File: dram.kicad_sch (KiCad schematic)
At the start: 21 parts, among them J2 74157, J3 74157, J7 74LS280, K10 74LS08, K9 4164, U10 4164, U11 4164, U12 4164, U13 4164, U4 74LS04, U6 4164, U7 4164, U8 4164, U9 4164

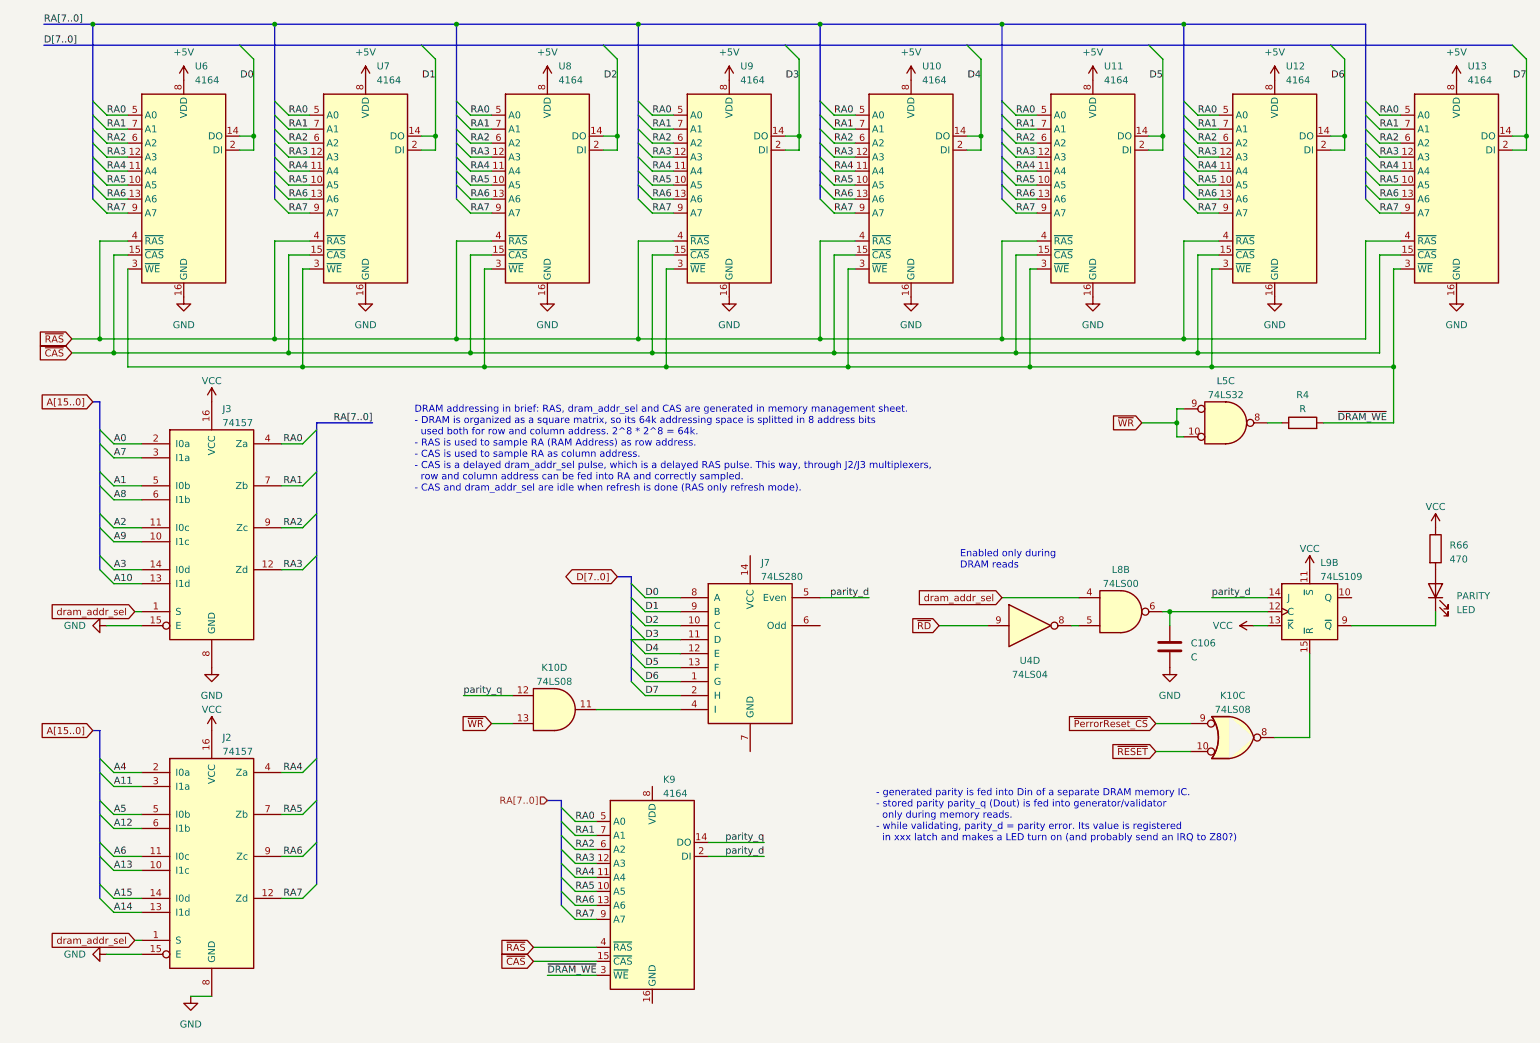
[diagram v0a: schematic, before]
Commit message: Components renaming according to the Uxy convention.
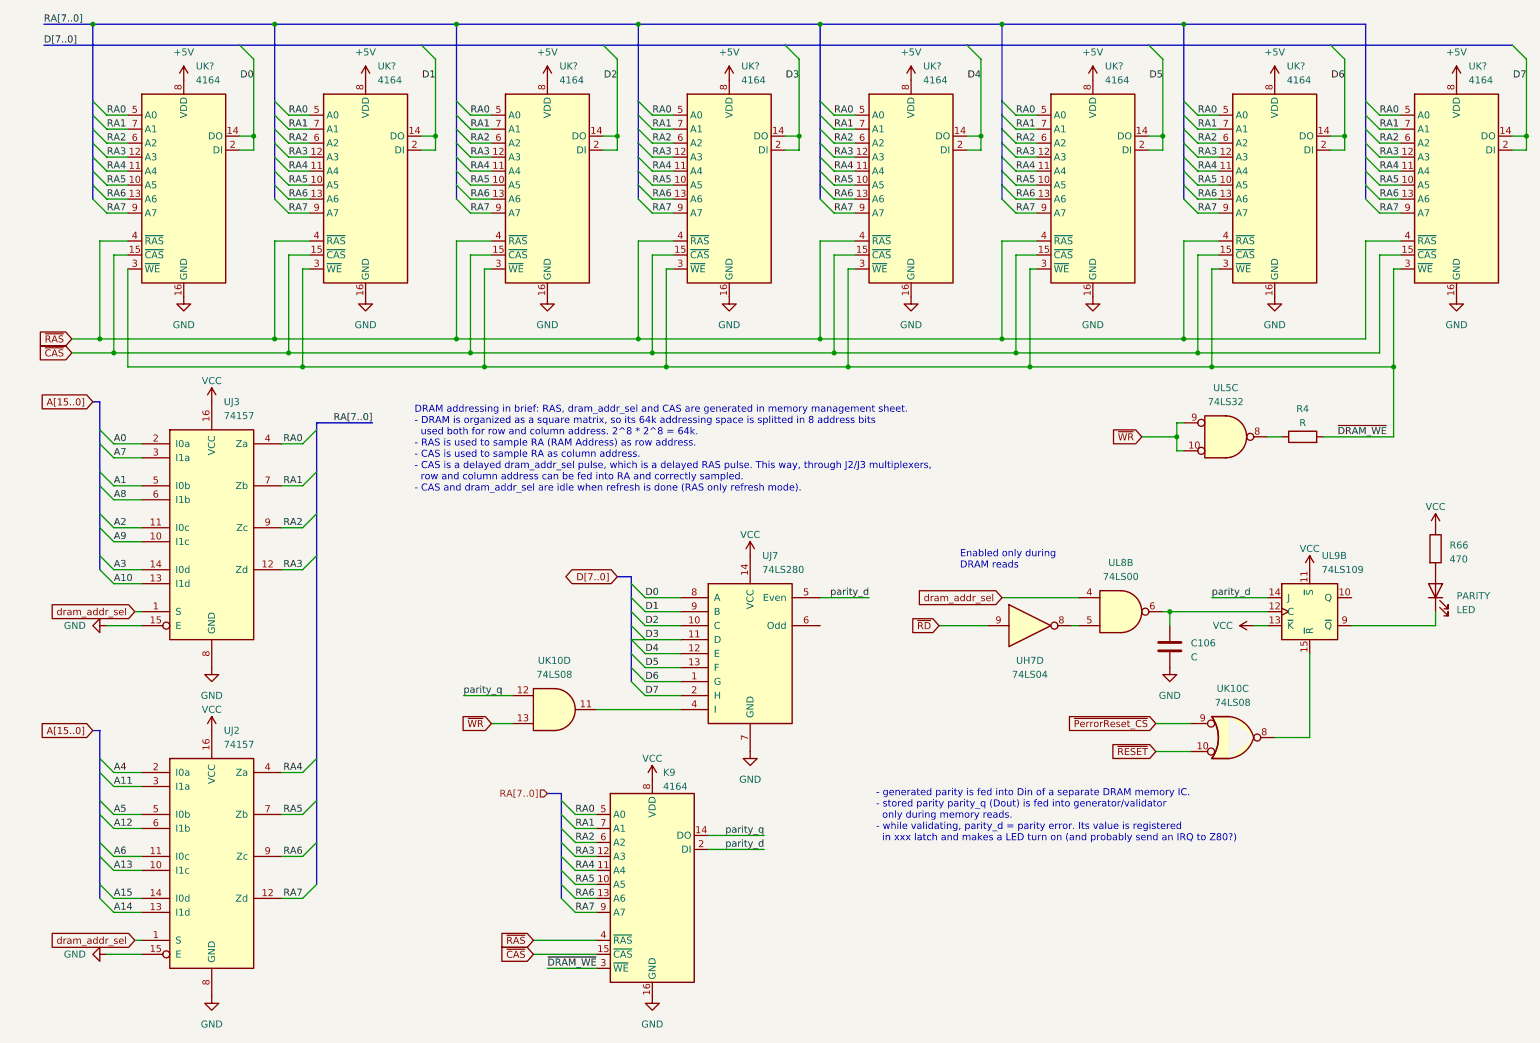
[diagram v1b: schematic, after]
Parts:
- renumbered U4 to UH7, J2 to UJ2, J3 to UJ3, J7 to UJ7, K10 to UK10, U7 to UK?, U13 to UK?, U10 to UK?, U11 to UK?, U12 to UK?, U9 to UK?, U8 to UK?, U6 to UK?, L5 to UL5, L8 to UL8, L9 to UL9
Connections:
- net GND: now also K9.16 (GND), UJ7.7 (GND)
- net VCC: now also K9.8 (VDD), UJ7.14 (VCC)
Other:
- moved on the sheet: K9, R4, UL5C

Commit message: VCC -> +5V
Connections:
- net VCC is gone; now on net +5V: K9.8 (VDD), R66.1, UJ2.16 (VCC), UJ3.16 (VCC), UJ7.14 (VCC), UL9.11 (~{S}), UL9.13 (~{K})
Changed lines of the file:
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@@
     )
   )
-  (symbol (lib_id "power:VCC") (at 233.68 124.46 90) (unit 1)
-    (in_bom yes) (on_board yes) (dnp no) (fields_autoplaced)
-    (property "Reference" "#PWR010" (at 237.49 124.46 0)
-      (effects (font (size 1.27 1.27)) hide)
-    )
-    (property "Value" "VCC" (at 229.87 124.46 90)
+  (symbol (lib_name "+5V_1") (lib_id "power:+5V") (at 233.68 124.46 90) (unit 1)
+    (in_bom yes) (on_board yes) (dnp no) (fields_autoplaced)
+    (property "Reference" "#PWR?" (at 237.49 124.46 0)
+      (effects (font (size 1.27 1.27)) hide)
+    )
+    (property "Value" "+5V" (at 229.87 124.46 90)
       (effects (font (size 1.27 1.27)) (justify left))
     )
@@
       (project "ceda"
         (path "/12a6dbe3-008d-4c5b-88f6-9f1c816060be/f05e0b09-5f96-4638-8985-dbb50d0f6ef2"
-          (reference "#PWR010") (unit 1)
+          (reference "#PWR?") (unit 1)
         )
       )
@@
     )
   )
-  (symbol (lib_id "power:VCC") (at 44.45 143.51 0) (unit 1)
-    (in_bom yes) (on_board yes) (dnp no) (fields_autoplaced)
-    (property "Reference" "#PWR031" (at 44.45 147.32 0)
-      (effects (font (size 1.27 1.27)) hide)
-    )
-    (property "Value" "VCC" (at 44.45 139.7 0)
+  (symbol (lib_name "+5V_2") (lib_id "power:+5V") (at 44.45 143.51 0) (unit 1)
+    (in_bom yes) (on_board yes) (dnp no) (fields_autoplaced)
+    (property "Reference" "#PWR?" (at 44.45 147.32 0)
+      (effects (font (size 1.27 1.27)) hide)
+    )
+    (property "Value" "+5V" (at 44.45 138.43 0)
       (effects (font (size 1.27 1.27)))
     )
@@
       (project "ceda"
         (path "/12a6dbe3-008d-4c5b-88f6-9f1c816060be/f05e0b09-5f96-4638-8985-dbb50d0f6ef2"
-          (reference "#PWR031") (unit 1)
+          (reference "#PWR?") (unit 1)
         )
       )
@@
     )
   )
-  (symbol (lib_id "power:VCC") (at 44.45 83.82 0) (unit 1)
-    (in_bom yes) (on_board yes) (dnp no) (fields_autoplaced)
-    (property "Reference" "#PWR030" (at 44.45 87.63 0)
-      (effects (font (size 1.27 1.27)) hide)
-    )
-    (property "Value" "VCC" (at 44.45 80.01 0)
+  (symbol (lib_name "+5V_3") (lib_id "power:+5V") (at 44.45 83.82 0) (unit 1)
+    (in_bom yes) (on_board yes) (dnp no) (fields_autoplaced)
+    (property "Reference" "#PWR?" (at 44.45 87.63 0)
+      (effects (font (size 1.27 1.27)) hide)
+    )
+    (property "Value" "+5V" (at 44.45 78.74 0)
       (effects (font (size 1.27 1.27)))
     )
@@
       (project "ceda"
         (path "/12a6dbe3-008d-4c5b-88f6-9f1c816060be/f05e0b09-5f96-4638-8985-dbb50d0f6ef2"
-          (reference "#PWR030") (unit 1)
-        )
-      )
-    )
-  )
-  (symbol (lib_id "power:VCC") (at 266.7 106.68 0) (unit 1)
-    (in_bom yes) (on_board yes) (dnp no) (fields_autoplaced)
-    (property "Reference" "#PWR011" (at 266.7 110.49 0)
-      (effects (font (size 1.27 1.27)) hide)
-    )
-    (property "Value" "VCC" (at 266.7 102.87 0)
+          (reference "#PWR?") (unit 1)
+        )
+      )
+    )
+  )
+  (symbol (lib_name "+5V_4") (lib_id "power:+5V") (at 266.7 106.68 0) (unit 1)
+    (in_bom yes) (on_board yes) (dnp no) (fields_autoplaced)
+    (property "Reference" "#PWR?" (at 266.7 110.49 0)
+      (effects (font (size 1.27 1.27)) hide)
+    )
+    (property "Value" "+5V" (at 266.7 101.6 0)
       (effects (font (size 1.27 1.27)))
     )
@@
       (project "ceda"
         (path "/12a6dbe3-008d-4c5b-88f6-9f1c816060be/f05e0b09-5f96-4638-8985-dbb50d0f6ef2"
-          (reference "#PWR011") (unit 1)
+          (reference "#PWR?") (unit 1)
         )
       )
@@
     )
   )
-  (symbol (lib_id "power:VCC") (at 142.24 111.76 0) (unit 1)
-    (in_bom yes) (on_board yes) (dnp no) (fields_autoplaced)
-    (property "Reference" "#PWR0235" (at 142.24 115.57 0)
-      (effects (font (size 1.27 1.27)) hide)
-    )
-    (property "Value" "VCC" (at 142.24 107.95 0)
+  (symbol (lib_name "+5V_6") (lib_id "power:+5V") (at 142.24 111.76 0) (unit 1)
+    (in_bom yes) (on_board yes) (dnp no) (fields_autoplaced)
+    (property "Reference" "#PWR?" (at 142.24 115.57 0)
+      (effects (font (size 1.27 1.27)) hide)
+    )
+    (property "Value" "+5V" (at 142.24 106.68 0)
       (effects (font (size 1.27 1.27)))
     )
@@
       (project "ceda"
         (path "/12a6dbe3-008d-4c5b-88f6-9f1c816060be/f05e0b09-5f96-4638-8985-dbb50d0f6ef2"
-          (reference "#PWR0235") (unit 1)
+          (reference "#PWR?") (unit 1)
         )
       )
@@
     )
   )
-  (symbol (lib_id "power:VCC") (at 243.84 114.3 0) (unit 1)
-    (in_bom yes) (on_board yes) (dnp no) (fields_autoplaced)
-    (property "Reference" "#PWR012" (at 243.84 118.11 0)
-      (effects (font (size 1.27 1.27)) hide)
-    )
-    (property "Value" "VCC" (at 243.84 110.49 0)
+  (symbol (lib_name "+5V_5") (lib_id "power:+5V") (at 243.84 114.3 0) (unit 1)
+    (in_bom yes) (on_board yes) (dnp no) (fields_autoplaced)
+    (property "Reference" "#PWR?" (at 243.84 118.11 0)
+      (effects (font (size 1.27 1.27)) hide)
+    )
+    (property "Value" "+5V" (at 243.84 109.22 0)
       (effects (font (size 1.27 1.27)))
     )
@@
       (project "ceda"
         (path "/12a6dbe3-008d-4c5b-88f6-9f1c816060be/f05e0b09-5f96-4638-8985-dbb50d0f6ef2"
-          (reference "#PWR012") (unit 1)
+          (reference "#PWR?") (unit 1)
         )
       )
@@
     )
   )
-  (symbol (lib_id "power:VCC") (at 124.46 152.4 0) (unit 1)
-    (in_bom yes) (on_board yes) (dnp no) (fields_autoplaced)
-    (property "Reference" "#PWR0236" (at 124.46 156.21 0)
-      (effects (font (size 1.27 1.27)) hide)
-    )
-    (property "Value" "VCC" (at 124.46 148.59 0)
+  (symbol (lib_name "+5V_7") (lib_id "power:+5V") (at 124.46 152.4 0) (unit 1)
+    (in_bom yes) (on_board yes) (dnp no) (fields_autoplaced)
+    (property "Reference" "#PWR?" (at 124.46 156.21 0)
+      (effects (font (size 1.27 1.27)) hide)
+    )
+    (property "Value" "+5V" (at 124.46 147.32 0)
       (effects (font (size 1.27 1.27)))
     )
@@
       (project "ceda"
         (path "/12a6dbe3-008d-4c5b-88f6-9f1c816060be/f05e0b09-5f96-4638-8985-dbb50d0f6ef2"
-          (reference "#PWR0236") (unit 1)
-        )
-      )
+          (reference "#PWR?") (unit 1)
+        )
+      )

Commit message: Notes in kicad's sheet text blocks
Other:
- company: (none) -> Logic Systems Int'l Inc
- title: (none) -> CEDA - Sanco 8003 schematics
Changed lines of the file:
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@@
 (kicad_sch (version 20230121) (generator eeschema)
   (paper "A4")
+  (title_block
+    (title "CEDA - Sanco 8003 schematics")
+    (rev "05")
+    (company "Logic Systems Int'l Inc")
+    (comment 1 "reversed by RetrOfficina - retrofficina.glgprograms.it")
+    (comment 3 "Dynamic RAM addressing and parity handling")
+    (comment 4 "DRAM")
+  )
   (junction (at 154.94 15.24) (diameter 0) (color 0 0 0 0)
   )

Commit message: Annotated all components
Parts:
- gave numbers to parts that had none: 8
- renumbered PARITY to PARITY1
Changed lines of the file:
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@@
 		(dnp no)
 		(fields_autoplaced yes)
-		(property "Reference" "UK?"
+		(property "Reference" "UK2"
 			(at 74.5841 22.86 0)
 			(effects
@@
 			(project "ceda"
 				(path "/12a6dbe3-008d-4c5b-88f6-9f1c816060be/f05e0b09-5f96-4638-8985-dbb50d0f6ef2"
-					(reference "UK?")
+					(reference "UK2")
 					(unit 1)
 				)
@@
 		(dnp no)
 		(fields_autoplaced yes)
-		(property "Reference" "UK?"
+		(property "Reference" "UK8"
 			(at 272.7041 22.86 0)
 			(effects
@@
 			(project "ceda"
 				(path "/12a6dbe3-008d-4c5b-88f6-9f1c816060be/f05e0b09-5f96-4638-8985-dbb50d0f6ef2"
-					(reference "UK?")
+					(reference "UK8")
 					(unit 1)
 				)
@@
 		(dnp no)
 		(fields_autoplaced yes)
-		(property "Reference" "UK?"
+		(property "Reference" "UK5"
 			(at 173.6441 22.86 0)
 			(effects
@@
 			(project "ceda"
 				(path "/12a6dbe3-008d-4c5b-88f6-9f1c816060be/f05e0b09-5f96-4638-8985-dbb50d0f6ef2"
-					(reference "UK?")
+					(reference "UK5")
 					(unit 1)
 				)
@@
 		(dnp no)
 		(fields_autoplaced yes)
-		(property "Reference" "UK?"
+		(property "Reference" "UK6"
 			(at 206.6641 22.86 0)
 			(effects
@@
 			(project "ceda"
 				(path "/12a6dbe3-008d-4c5b-88f6-9f1c816060be/f05e0b09-5f96-4638-8985-dbb50d0f6ef2"
-					(reference "UK?")
+					(reference "UK6")
 					(unit 1)
 				)
@@
 		(dnp no)
 		(fields_autoplaced yes)
-		(property "Reference" "UK?"
+		(property "Reference" "UK7"
 			(at 239.6841 22.86 0)
 			(effects
@@
 			(project "ceda"
 				(path "/12a6dbe3-008d-4c5b-88f6-9f1c816060be/f05e0b09-5f96-4638-8985-dbb50d0f6ef2"
-					(reference "UK?")
+					(reference "UK7")
 					(unit 1)
 				)
@@
 		(dnp no)
 		(fields_autoplaced yes)
-		(property "Reference" "UK?"
+		(property "Reference" "UK4"
 			(at 140.6241 22.86 0)
 			(effects
@@
 			(project "ceda"
 				(path "/12a6dbe3-008d-4c5b-88f6-9f1c816060be/f05e0b09-5f96-4638-8985-dbb50d0f6ef2"
-					(reference "UK?")
+					(reference "UK4")
 					(unit 1)
 				)
@@
 		(dnp no)
 		(fields_autoplaced yes)
-		(property "Reference" "UK?"
+		(property "Reference" "UK3"
 			(at 107.6041 22.86 0)
 			(effects
@@
 			(project "ceda"
 				(path "/12a6dbe3-008d-4c5b-88f6-9f1c816060be/f05e0b09-5f96-4638-8985-dbb50d0f6ef2"
-					(reference "UK?")
+					(reference "UK3")
 					(unit 1)
 				)
@@
 		(dnp no)
 		(fields_autoplaced yes)
-		(property "Reference" "UK?"
+		(property "Reference" "UK1"
 			(at 41.5641 22.86 0)
 			(effects
@@
 			(project "ceda"
 				(path "/12a6dbe3-008d-4c5b-88f6-9f1c816060be/f05e0b09-5f96-4638-8985-dbb50d0f6ef2"
-					(reference "UK?")
+					(reference "UK1")
 					(unit 1)
 				)
@@
 		(dnp no)
 		(fields_autoplaced yes)
-		(property "Reference" "PARITY"
+		(property "Reference" "PARITY1"
 			(at 270.51 119.0625 90)
 			(effects
@@
 			(project "ceda"
 				(path "/12a6dbe3-008d-4c5b-88f6-9f1c816060be/f05e0b09-5f96-4638-8985-dbb50d0f6ef2"
-					(reference "PARITY")
+					(reference "PARITY1")
 					(unit 1)
 				)

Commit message: Assigned default footprints to ICs
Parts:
- UH7, UJ7, UK10, UL5, UL8: footprint (none) -> Package_DIP:DIP-14_W7.62mm
- UJ2, UJ3, UL9: footprint (none) -> Package_DIP:DIP-16_W7.62mm
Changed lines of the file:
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@@
 			)
 		)
-		(property "Footprint" ""
+		(property "Footprint" "Package_DIP:DIP-16_W7.62mm"
 			(at 44.45 166.37 0)
 			(effects
@@
 			)
 		)
-		(property "Footprint" ""
+		(property "Footprint" "Package_DIP:DIP-16_W7.62mm"
 			(at 243.84 121.92 0)
 			(effects
@@
 			)
 		)
-		(property "Footprint" ""
+		(property "Footprint" "Package_DIP:DIP-14_W7.62mm"
 			(at 106.68 139.7 0)
 			(effects
@@
 			)
 		)
-		(property "Footprint" ""
+		(property "Footprint" "Package_DIP:DIP-16_W7.62mm"
 			(at 44.45 106.68 0)
 			(effects
@@
 			)
 		)
-		(property "Footprint" ""
+		(property "Footprint" "Package_DIP:DIP-14_W7.62mm"
 			(at 142.24 129.54 0)
 			(effects
@@
 			)
 		)
-		(property "Footprint" ""
+		(property "Footprint" "Package_DIP:DIP-14_W7.62mm"
 			(at 229.87 144.78 0)
 			(effects
@@
 			)
 		)
-		(property "Footprint" ""
+		(property "Footprint" "Package_DIP:DIP-14_W7.62mm"
 			(at 193.04 124.46 0)
 			(effects
@@
 			)
 		)
-		(property "Footprint" ""
+		(property "Footprint" "Package_DIP:DIP-14_W7.62mm"
 			(at 209.55 121.92 0)
 			(effects
@@
 			)
 		)
-		(property "Footprint" ""
+		(property "Footprint" "Package_DIP:DIP-14_W7.62mm"
 			(at 228.6 90.17 0)
 			(effects

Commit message: Fixed packages
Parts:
- K9, UK1, UK2, UK3, UK4, UK5, UK6, UK7, UK8: footprint Package_DIP:DIP-16_W7.62mm_LongPads -> Package_DIP:DIP-16_W7.62mm
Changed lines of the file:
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@@
 			)
 		)
-		(property "Footprint" "Package_DIP:DIP-16_W7.62mm_LongPads"
+		(property "Footprint" "Package_DIP:DIP-16_W7.62mm"
 			(at 124.46 204.47 0)
 			(effects
@@
 			)
 		)
-		(property "Footprint" "Package_DIP:DIP-16_W7.62mm_LongPads"
+		(property "Footprint" "Package_DIP:DIP-16_W7.62mm"
 			(at 72.39 77.47 0)
 			(effects
@@
 			)
 		)
-		(property "Footprint" "Package_DIP:DIP-16_W7.62mm_LongPads"
+		(property "Footprint" "Package_DIP:DIP-16_W7.62mm"
 			(at 270.51 77.47 0)
 			(effects
@@
 			)
 		)
-		(property "Footprint" "Package_DIP:DIP-16_W7.62mm_LongPads"
+		(property "Footprint" "Package_DIP:DIP-16_W7.62mm"
 			(at 171.45 77.47 0)
 			(effects
@@
 			)
 		)
-		(property "Footprint" "Package_DIP:DIP-16_W7.62mm_LongPads"
+		(property "Footprint" "Package_DIP:DIP-16_W7.62mm"
 			(at 204.47 77.47 0)
 			(effects
@@
 			)
 		)
-		(property "Footprint" "Package_DIP:DIP-16_W7.62mm_LongPads"
+		(property "Footprint" "Package_DIP:DIP-16_W7.62mm"
 			(at 237.49 77.47 0)
 			(effects
@@
 			)
 		)
-		(property "Footprint" "Package_DIP:DIP-16_W7.62mm_LongPads"
+		(property "Footprint" "Package_DIP:DIP-16_W7.62mm"
 			(at 138.43 77.47 0)
 			(effects
@@
 			)
 		)
-		(property "Footprint" "Package_DIP:DIP-16_W7.62mm_LongPads"
+		(property "Footprint" "Package_DIP:DIP-16_W7.62mm"
 			(at 105.41 77.47 0)
 			(effects
@@
 			)
 		)
-		(property "Footprint" "Package_DIP:DIP-16_W7.62mm_LongPads"
+		(property "Footprint" "Package_DIP:DIP-16_W7.62mm"
 			(at 39.37 77.47 0)
 			(effects
